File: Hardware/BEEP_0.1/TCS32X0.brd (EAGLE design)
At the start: 29.6 x 37.3 mm, 15 parts, among them IC1 TCS32X0

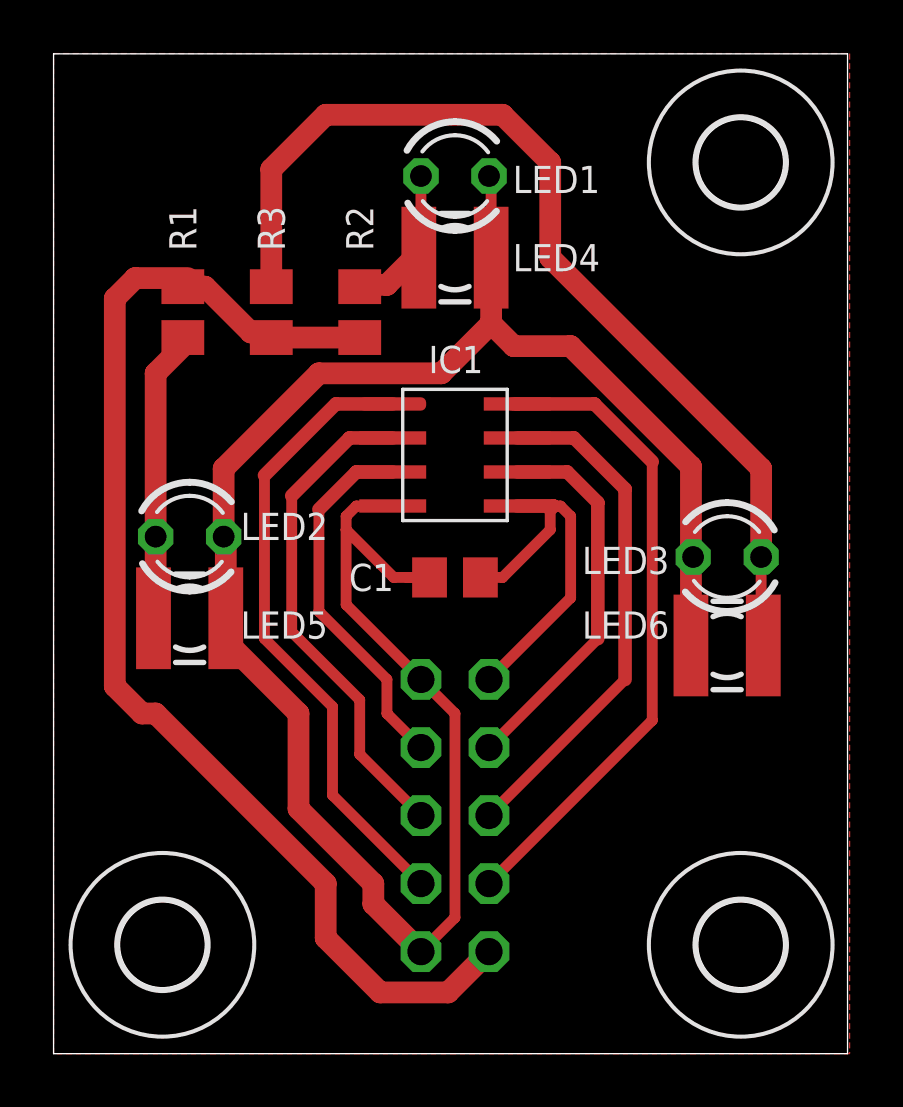
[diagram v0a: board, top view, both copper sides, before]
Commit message: enlarge Clearence to 10mil created some pdf files for the boards
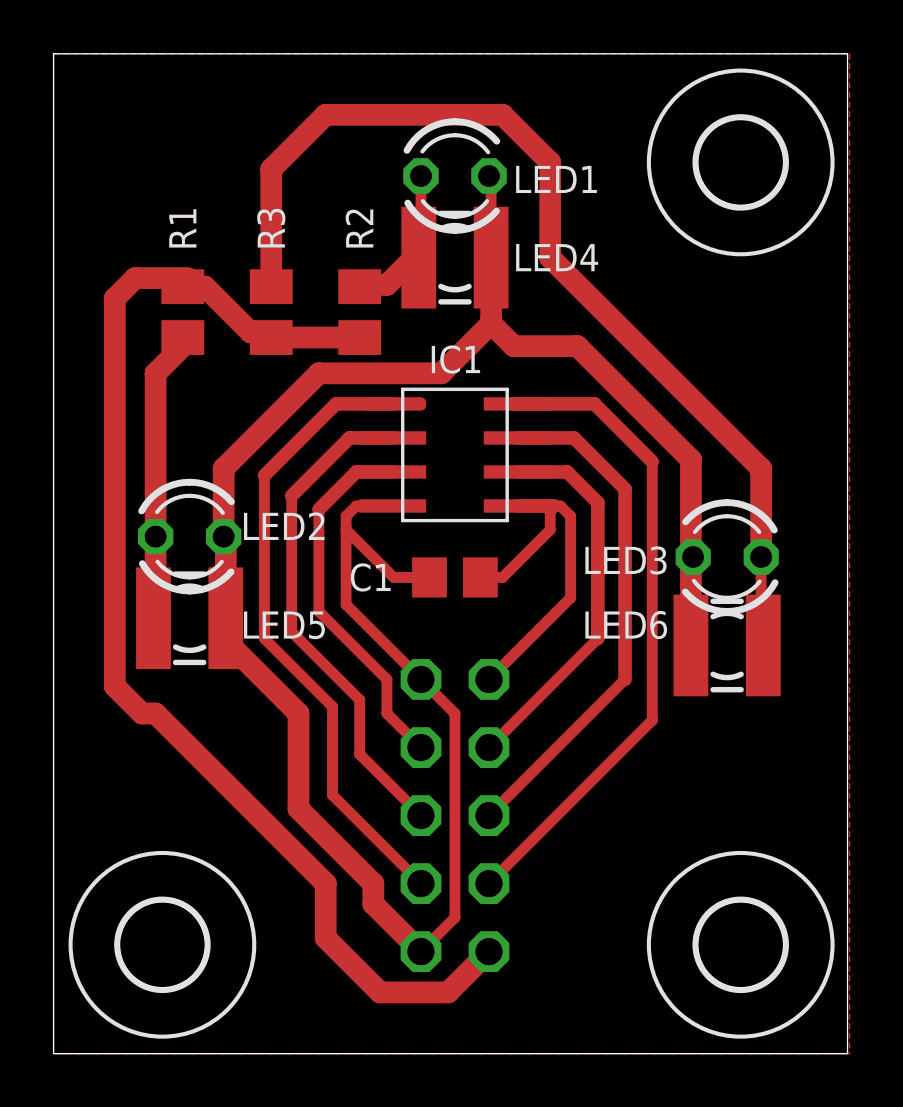
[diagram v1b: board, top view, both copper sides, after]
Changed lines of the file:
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@@
 </class>
 </classes>
-<designrules name="default">
+<designrules name="default *">
 <description language="de">&lt;b&gt;EAGLE Design Rules&lt;/b&gt;
 &lt;p&gt;
@@
 <param name="mtCopper" value="0.035mm 0.035mm 0.035mm 0.035mm 0.035mm 0.035mm 0.035mm 0.035mm 0.035mm 0.035mm 0.035mm 0.035mm 0.035mm 0.035mm 0.035mm 0.035mm"/>
 <param name="mtIsolate" value="1.5mm 0.15mm 0.2mm 0.15mm 0.2mm 0.15mm 0.2mm 0.15mm 0.2mm 0.15mm 0.2mm 0.15mm 0.2mm 0.15mm 0.2mm"/>
-<param name="mdWireWire" value="8mil"/>
-<param name="mdWirePad" value="8mil"/>
+<param name="mdWireWire" value="10mil"/>
+<param name="mdWirePad" value="10mil"/>
 <param name="mdWireVia" value="8mil"/>
 <param name="mdPadPad" value="8mil"/>
@@
 <wire x1="9.906" y1="25.4" x2="6.35" y2="21.844" width="0.8128" layer="1"/>
 <wire x1="6.35" y1="21.844" x2="6.35" y2="19.304" width="0.8128" layer="1"/>
-<wire x1="23.796" y1="15.24" x2="23.796" y2="21.924" width="0.8128" layer="1"/>
-<wire x1="23.796" y1="21.924" x2="19.304" y2="26.416" width="0.8128" layer="1"/>
-<wire x1="19.304" y1="26.416" x2="17.178" y2="26.416" width="0.8128" layer="1"/>
+<wire x1="23.796" y1="15.24" x2="23.796" y2="22.178" width="0.8128" layer="1"/>
+<wire x1="23.796" y1="22.178" x2="19.558" y2="26.416" width="0.8128" layer="1"/>
+<wire x1="19.558" y1="26.416" x2="17.178" y2="26.416" width="0.8128" layer="1"/>
 <wire x1="17.178" y1="26.416" x2="16.336" y2="27.258" width="0.8128" layer="1"/>
 <wire x1="23.796" y1="15.24" x2="23.796" y2="18.462" width="0.4064" layer="1"/>

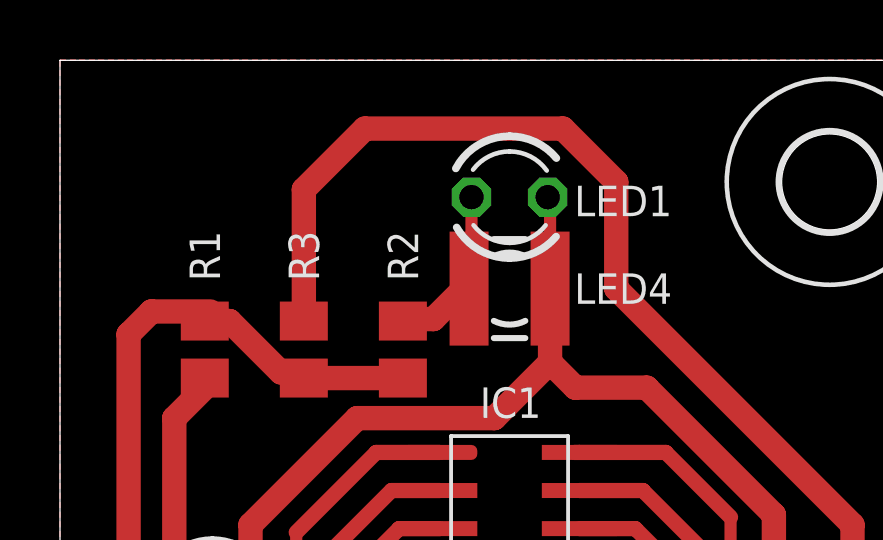
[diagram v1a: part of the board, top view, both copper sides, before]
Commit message: Add branding ;) enhance PCBs finish Easy RGB Board add Texas Instruments libray from Element 14 add dxf import ulp for eagle add Script for easy eagle export to pdf for etching minor cleanup
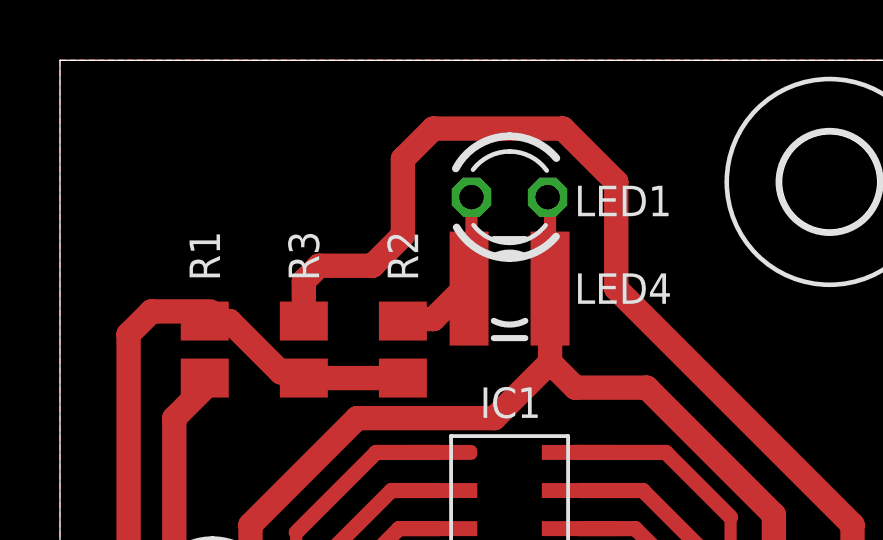
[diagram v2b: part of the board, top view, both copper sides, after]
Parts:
- added U$1: LOGO-COPPER4, Branding:COPPER4
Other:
- board text added: "TCS32X0 v0.1.1"
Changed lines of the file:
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@@
 <layer number="43" name="vRestrict" color="2" fill="10" visible="yes" active="yes"/>
 <layer number="44" name="Drills" color="7" fill="1" visible="no" active="yes"/>
-<layer number="45" name="Holes" color="7" fill="1" visible="no" active="yes"/>
+<layer number="45" name="Holes" color="7" fill="1" visible="yes" active="yes"/>
 <layer number="46" name="Milling" color="3" fill="1" visible="no" active="yes"/>
 <layer number="47" name="Measures" color="7" fill="1" visible="no" active="yes"/>
-<layer number="48" name="Document" color="7" fill="1" visible="yes" active="yes"/>
-<layer number="49" name="Reference" color="7" fill="1" visible="yes" active="yes"/>
+<layer number="48" name="Document" color="7" fill="1" visible="no" active="yes"/>
+<layer number="49" name="Reference" color="7" fill="1" visible="no" active="yes"/>
 <layer number="51" name="tDocu" color="7" fill="1" visible="yes" active="yes"/>
 <layer number="52" name="bDocu" color="7" fill="1" visible="yes" active="yes"/>
@@
 <layer number="97" name="Info" color="7" fill="1" visible="no" active="no"/>
 <layer number="98" name="Guide" color="6" fill="1" visible="no" active="no"/>
+<layer number="100" name="tCName" color="7" fill="1" visible="yes" active="yes"/>
+<layer number="101" name="bCName" color="7" fill="1" visible="yes" active="yes"/>
 </layers>
 <board>
@@
 <text x="12.192" y="8.89" size="1.016" layer="26" rot="MR0" align="center-left">S1</text>
 <text x="12.192" y="11.43" size="1.016" layer="26" rot="MR0" align="center-left">NOE</text>
+<text x="1.016" y="31.496" size="1.016" layer="100">TCS32X0
+v0.1.1</text>
+<polygon width="0.8128" layer="41">
+<vertex x="0" y="31.242"/>
+<vertex x="4.572" y="31.242"/>
+<vertex x="4.572" y="32.512"/>
+<vertex x="9.398" y="32.512"/>
+<vertex x="9.398" y="37.338"/>
+<vertex x="0" y="37.338"/>
+</polygon>
 </plain>
 <attributes>
@@
 <attribute name="NAME" x="22.987" y="16.002" size="1.016" layer="25" align="center-right"/>
 </element>
+<element name="U$1" library="Branding" package="COPPER4" value="LOGO-COPPER4" x="1.016" y="34.544"/>
 </elements>
 <signals>
@@
 <contactref element="LED3" pad="A"/>
 <wire x1="18.542" y1="33.274" x2="16.764" y2="35.052" width="0.8128" layer="1"/>
-<wire x1="16.764" y1="35.052" x2="10.16" y2="35.052" width="0.8128" layer="1"/>
-<wire x1="10.16" y1="35.052" x2="8.128" y2="33.02" width="0.8128" layer="1"/>
-<wire x1="8.128" y1="33.02" x2="8.128" y2="28.636" width="0.8128" layer="1"/>
 <contactref element="LED6" pad="A"/>
 <wire x1="26.416" y1="18.542" x2="26.416" y2="15.32" width="0.4064" layer="1"/>
@@
 <wire x1="26.416" y1="21.844" x2="18.542" y2="29.718" width="0.8128" layer="1"/>
 <wire x1="18.542" y1="29.718" x2="18.542" y2="33.274" width="0.8128" layer="1"/>
+<wire x1="8.128" y1="28.636" x2="8.128" y2="29.972" width="0.8128" layer="1"/>
+<wire x1="8.128" y1="29.972" x2="8.636" y2="30.48" width="0.8128" layer="1"/>
+<wire x1="8.636" y1="30.48" x2="10.414" y2="30.48" width="0.8128" layer="1"/>
+<wire x1="10.414" y1="30.48" x2="11.43" y2="31.496" width="0.8128" layer="1"/>
+<wire x1="11.43" y1="31.496" x2="11.43" y2="34.036" width="0.8128" layer="1"/>
+<wire x1="11.43" y1="34.036" x2="12.446" y2="35.052" width="0.8128" layer="1"/>
+<wire x1="12.446" y1="35.052" x2="16.764" y2="35.052" width="0.8128" layer="1"/>
 </signal>
 <signal name="N$12">
@@
 </board>
 </drawing>
+<compatibility>
+<note version="6.3" minversion="6.2.2" severity="warning">
+Since Version 6.2.2 text objects can contain more than one line,
+which will not be processed correctly with this version.
+</note>
+</compatibility>
 </eagle>
